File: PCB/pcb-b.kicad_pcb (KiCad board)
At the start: 2 copper layers, 117.6 x 58.2 mm, 81 parts, among them Q1 BC817, Q10 BC817, Q12 BC817, Q14 BC817, Q15 BC817, Q17 BC327, Q18 BC327, Q19 BC817, Q2 BC817, Q20 BC817, Q21 BC817, Q3 BC817, Q4 IRF4905, Q5 IRF4905, Q6 IRF4905, Q7 IRF4905, Q8 IRF4905, Q9 IRF4905, U1 L7805, U2 L7805, U3 L7805, U4 HK19F-DC12-SHG

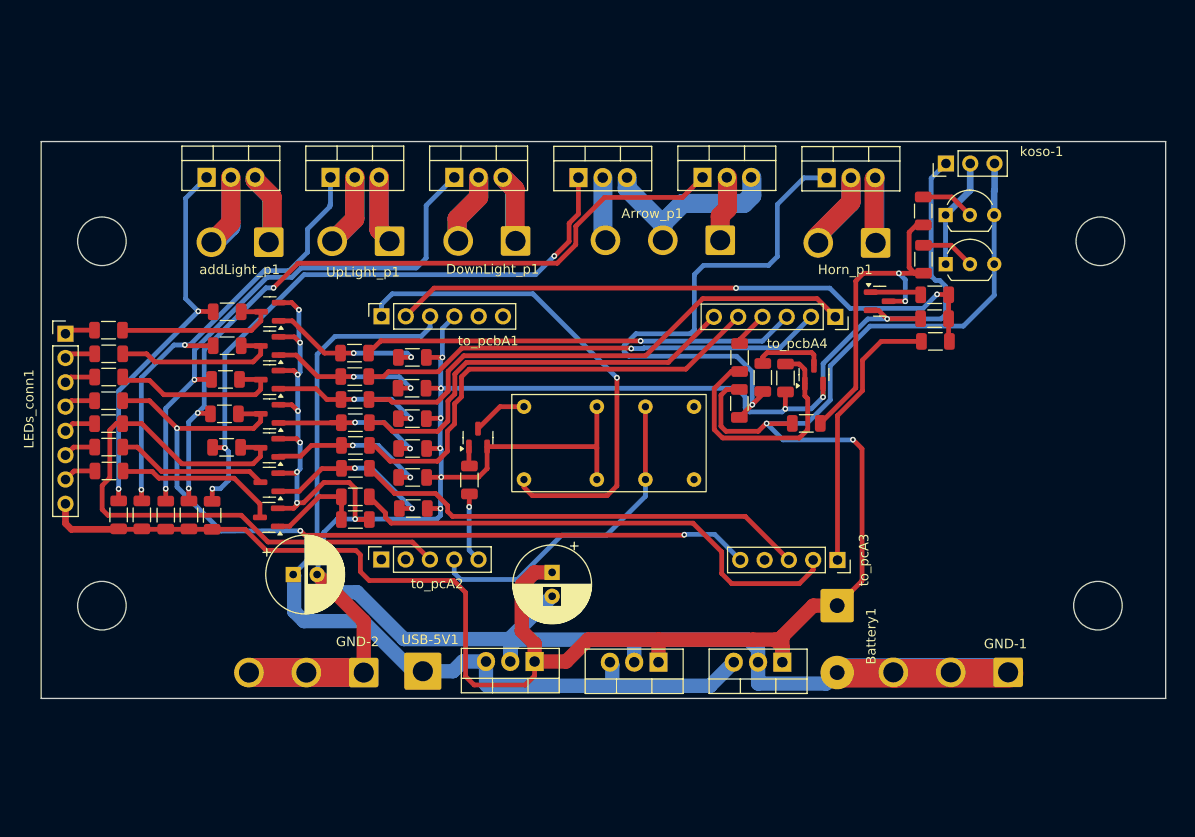
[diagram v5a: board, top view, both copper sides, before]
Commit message: SMD version using TPCA8120
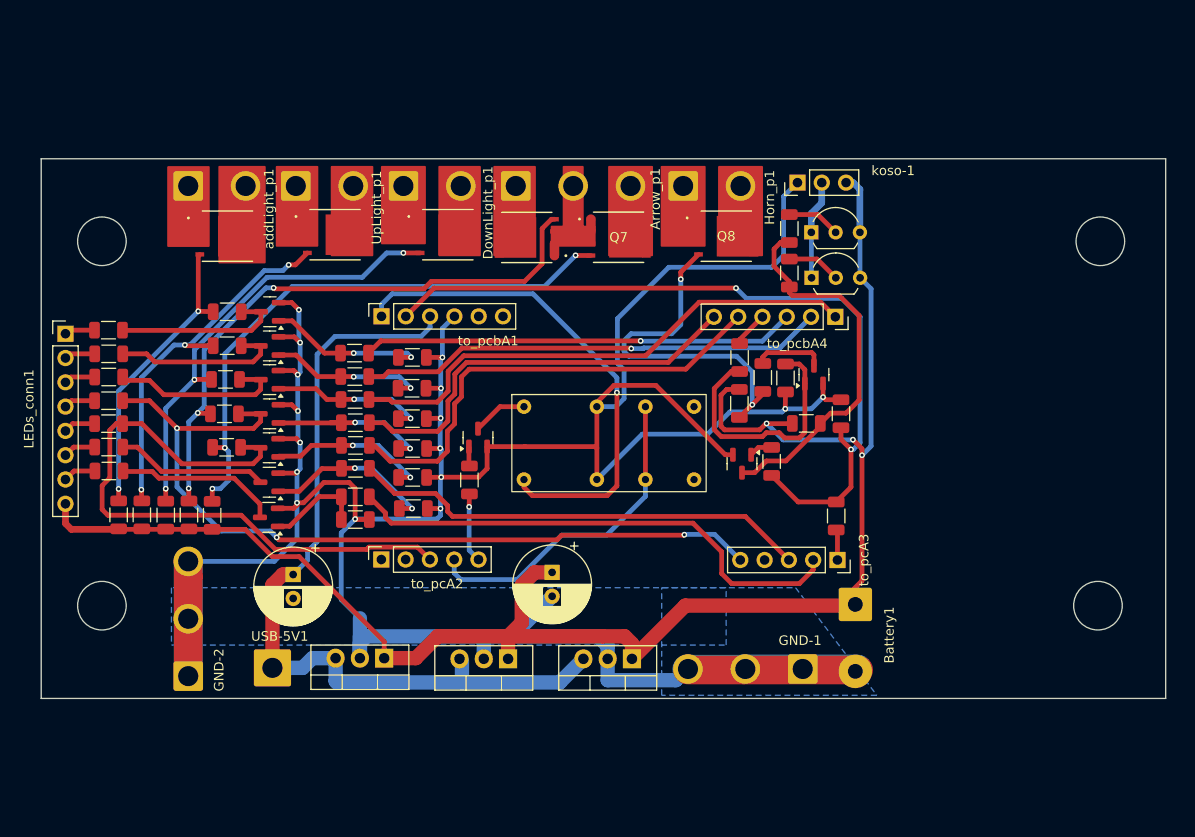
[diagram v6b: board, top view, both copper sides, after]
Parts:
- removed Q9: IRF4905, Package_TO_SOT_THT:TO-220-3_Vertical
- added Q11: TPCA8120,L1Q, TPCA8120:SOP Advance_TOS-L, F.Cu at (119.1, 78.3)
- Q4, Q5, Q6, Q7, Q8: value IRF4905 -> TPCA8120,L1Q; footprint Package_TO_SOT_THT:TO-220-3_Vertical -> TPCA8120:SOP Advance_TOS-L
- moved RA8 24.4 mm to (175.9, 101.9), turned to 90 degrees
- moved Q10 22.3 mm to (172.8, 102.1), turned to -90 degrees
- moved Arrow_p1 22.1 mm to (149.2, 73.1), turned to 0 degrees
- moved GND-1 21.5 mm to (179.2, 123.6)
- moved RA43 21.0 mm to (182.7, 107.6), turned to -90 degrees
- moved Horn_p1 21.0 mm to (166.7, 73.1), turned to 0 degrees
- moved GND-2 18.4 mm to (115.0, 124.3), turned to 90 degrees
- moved Q8 16.6 mm to (171.2, 78.3)
- moved U1 15.7 mm to (161.3, 122.5)
- moved U2 15.7 mm to (148.4, 122.5)
- moved U3 15.7 mm to (135.4, 122.5)
- moved USB-5V1 15.7 mm to (123.8, 123.5)
- moved koso-1 15.7 mm to (178.7, 72.8)
- moved Q4 14.7 mm to (130.3, 78.2)
- moved Q18 14.2 mm to (180.1, 78.0)
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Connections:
- Q4 pad 1: Net-(Q4-G) -> Net-(Q4-S_1)
- Q4 pad 2: Net-(Q4-D) -> Net-(Q4-S_1)
- Q4 pad 3: Net-(Q4-S) -> Net-(Q4-S_1)
- Q5 pad 1: Net-(Q5-G) -> Net-(DownLight_p1-Pin_1)
- Q5 pad 2: Net-(Q5-D) -> Net-(DownLight_p1-Pin_1)
- Q5 pad 3: Net-(Q5-S) -> Net-(DownLight_p1-Pin_1)
- Q6 pad 1: Net-(Q6-G) -> Net-(Arrow_p1-Pin_2)
- Q6 pad 2: Net-(DownLight_p1-Pin_2) -> Net-(Arrow_p1-Pin_2)
- Q6 pad 3: Net-(DownLight_p1-Pin_1) -> Net-(Arrow_p1-Pin_2)
- Q7 pad 1: Net-(Q7-G) -> Net-(Arrow_p1-Pin_2)
- Q7 pad 2: Net-(Arrow_p1-Pin_1) -> Net-(Arrow_p1-Pin_2)
- Q8 pad 1: Net-(Q8-G) -> Net-(Horn_p1-Pin_1)
- Q8 pad 2: Net-(Arrow_p1-Pin_3) -> Net-(Horn_p1-Pin_1)
- Q8 pad 3: Net-(Arrow_p1-Pin_2) -> Net-(Horn_p1-Pin_1)
- RA10 pad 2: Net-(Q4-G) -> Net-(Q11-G)
- RA11 pad 2: Net-(Q5-G) -> Net-(Q4-G)
- RA12 pad 2: Net-(Q6-G) -> Net-(Q5-G)
- RA13 pad 2: Net-(Q7-G) -> Net-(Q6-G)
- RA14 pad 2: Net-(Q8-G) -> Net-(Q7-G)
- RA15 pad 1: Net-(Q9-G) -> Net-(Q8-G)
- RA24 pad 2: Net-(Q4-G) -> Net-(Q11-G)
- RA25 pad 2: Net-(Q5-G) -> Net-(Q4-G)
- RA26 pad 2: Net-(Q6-G) -> Net-(Q5-G)
- RA27 pad 2: Net-(Q7-G) -> Net-(Q6-G)
- RA28 pad 2: Net-(Q8-G) -> Net-(Q7-G)
- RA42 pad 1: Net-(Q9-G) -> Net-(Q8-G)
- UpLight_p1 pad 1: Net-(Q5-S) -> Net-(Q4-S_1)
- UpLight_p1 pad 2: Net-(Q5-D) -> Net-(Q4-D_1)
- addLight_p1 pad 1: Net-(Q4-S) -> Net-(Q11-S_1)
- addLight_p1 pad 2: Net-(Q4-D) -> Net-(Q11-D_1)
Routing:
- net Net-(Q9-G): track 57.1 -> 0.00 mm, vias 1 -> 0
- net Net-(Q11-G): track 0.00 -> 31.0 mm, vias 0 -> 2
- net Net-(Q8-G): track 66.5 -> 37.3 mm, vias 3 -> 2
- net +12V: track 206.8 -> 179.3 mm, vias 2 -> 3
- net o_keepAlive: track 29.0 -> 3.20 mm
- net Net-(Arrow_p1-Pin_2): track 22.7 -> 2.54 mm
- net Net-(Q7-G): track 78.7 -> 60.7 mm
- net i_powerOFF: track 64.4 -> 81.1 mm
- net Net-(Q4-S): track 15.3 -> 0.00 mm
- net Net-(Q4-D): track 15.3 -> 0.00 mm
- net Net-(Q5-D): track 15.3 -> 0.00 mm
- net Net-(Q5-S): track 14.3 -> 0.00 mm
- net GND: track 360.4 -> 350.3 mm, vias 17 -> 16
- net Net-(Horn_p1-Pin_2): track 16.1 -> 7.73 mm
- net Net-(Q11-D_1): track 0.00 -> 7.98 mm
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- added copper zone on B.Cu, net GND
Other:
- board size 117.6 x 58.2 mm -> 117.6 x 56.4 mm

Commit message: Space optimization
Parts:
- moved Battery1 9.51 mm to (175.2, 116.3), turned to 0 degrees
- moved RA28 3.51 mm to (119.7, 104.8)
- moved RA27 3.43 mm to (117.2, 104.8)
- moved RA26 3.39 mm to (114.7, 104.8)
- moved RA25 3.37 mm to (112.2, 104.8)
- moved RA14 2.84 mm to (118.7, 97.6)
- moved C1 2.76 mm to (128.4, 112.6)
- moved GND-2 2.75 mm to (115.0, 121.6)
- moved RA24 2.35 mm to (106.7, 105.3), turned to 180 degrees
- moved RA13 2.33 mm to (118.7, 94.6)
- moved RA12 1.73 mm to (118.8, 91.6)
- moved C9 1.40 mm to (152.9, 112.1)
- moved RA11 1.20 mm to (119.0, 88.6)
- moved Arrow_p1 1.00 mm to (149.2, 74.1)
- moved DownLight_p1 1.00 mm to (137.4, 74.1)
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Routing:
- net Net-(Q5-G): track 47.0 -> 84.1 mm
- net c_rightArrow: track 66.4 -> 49.6 mm, vias 0 -> 2
- net tempPower: track 52.6 -> 36.8 mm
- net +12V: track 179.3 -> 193.1 mm, vias 3 -> 4
- net Net-(Q8-G): track 37.3 -> 27.1 mm
- net Net-(Q4-G): track 38.8 -> 34.0 mm
- net Net-(Q21-C): track 17.2 -> 20.8 mm
- net Net-(Q7-G): track 60.7 -> 57.4 mm
- net o_leftArrow: track 43.8 -> 46.4 mm
- net o_downLight: track 55.1 -> 57.4 mm
- net i_powerOFF: track 81.1 -> 83.3 mm
- net GND: track 350.3 -> 352.3 mm
- net +5V: track 91.0 -> 92.8 mm
- net o_rightArrow: track 48.6 -> 50.3 mm
- net Net-(Q20-C): track 15.9 -> 17.2 mm
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
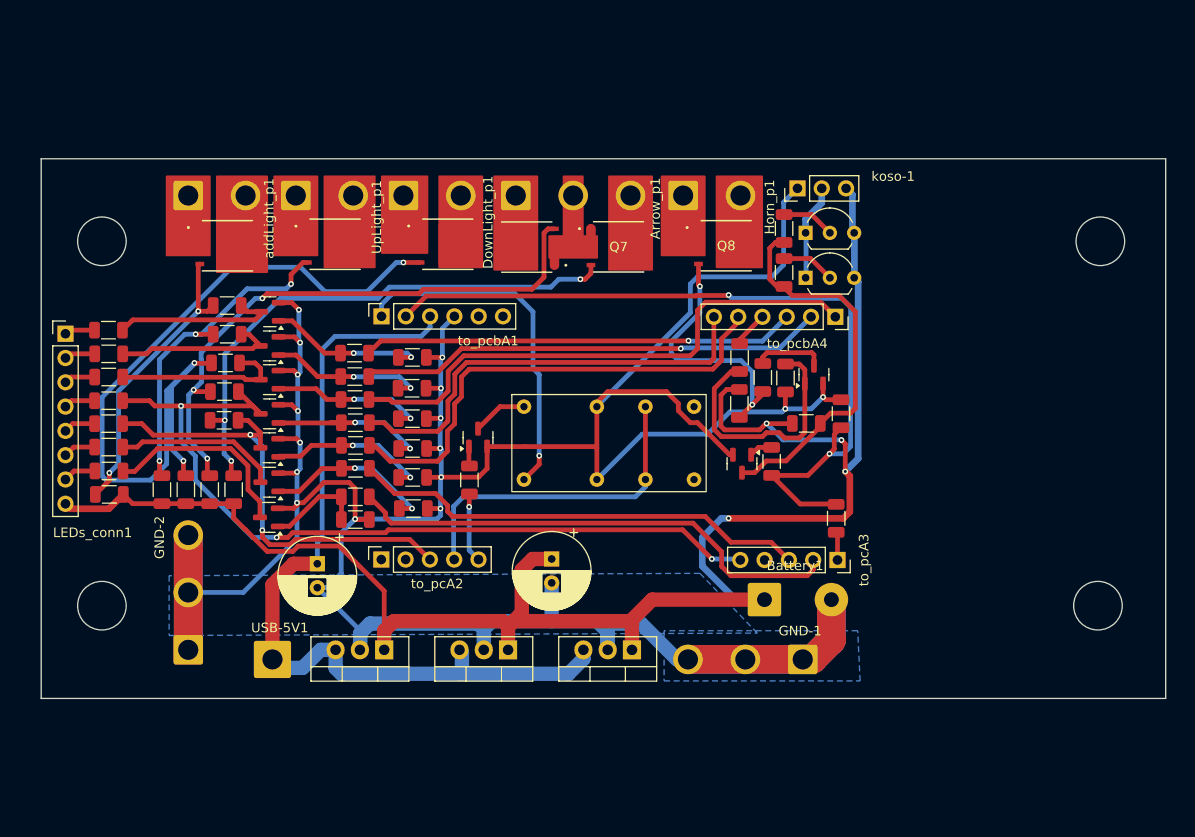
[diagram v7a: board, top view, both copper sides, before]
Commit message: Many changes
- The power drivers component has been implemented with TPCA8120 P-ch MOSfet
- The temp-power management has been moved from pcb-a to pcb-b
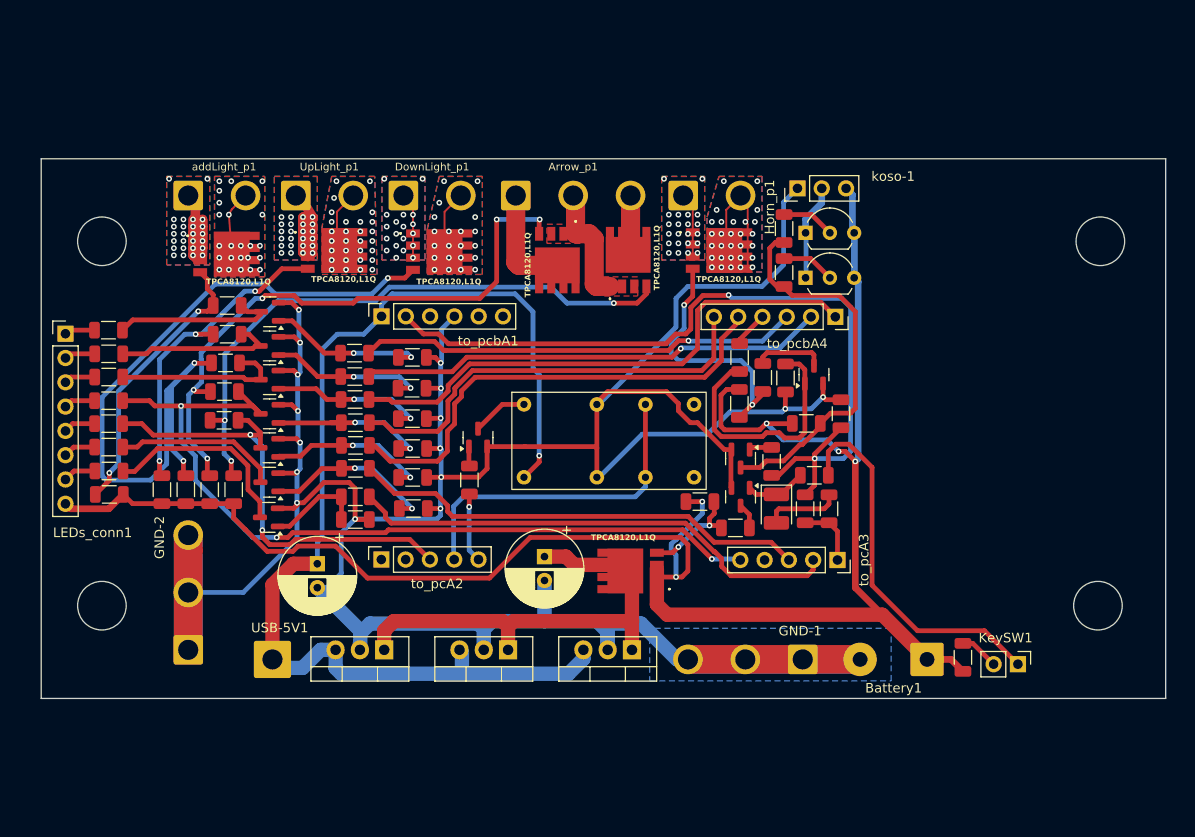
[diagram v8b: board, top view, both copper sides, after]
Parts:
- added D1: D_Small, Diode_SMD:D_1210_3225Metric_Pad1.42x2.65mm_HandSolder, F.Cu at (176.4, 106.8)
- added KeySW1: Conn_01x02, Connector_PinHeader_2.54mm:PinHeader_1x02_P2.54mm_Vertical, F.Cu at (201.7, 123.1)
- added Q13: TPCA8120,L1Q, TPCA8120:TPH4R003NLL1Q, F.Cu at (161.2, 113.3)
- added Q9: BC817, Package_TO_SOT_SMD:SOT-23, F.Cu at (172.7, 105.6)
- added R1: 5K, Resistor_SMD:R_1206_3216Metric, F.Cu at (195.9, 122.4)
- added R2: 10K, Resistor_SMD:R_1206_3216Metric, F.Cu at (168.4, 106.1)
- added R3: 33K, Resistor_SMD:R_1206_3216Metric, F.Cu at (172.2, 108.8)
- added R4: 5K, Resistor_SMD:R_1206_3216Metric, F.Cu at (180.4, 103.3)
- added R5: 5K, Resistor_SMD:R_1206_3216Metric, F.Cu at (181.9, 106.8)
- Q11, Q4, Q5, Q6, Q7, Q8: footprint TPCA8120:SOP Advance_TOS-L -> TPCA8120:TPH4R003NLL1Q
- RA10, RA11, RA12: value 240 -> 33K
- RA13, RA14: value 8K -> 33K
- RA15: value 8K -> 33k
- RA24, RA25, RA26, RA27, RA28: value 100K -> 10K
- RA42: value 8K -> 10k
- moved Battery1 18.1 mm to (192.2, 122.6), turned to 180 degrees
- moved Q6 3.48 mm to (153.5, 80.8)
- moved RA43 3.40 mm to (179.4, 106.8)
- moved Q7 1.71 mm to (160.9, 80.8)
- moved Q5 1.18 mm to (141.2, 80.0), turned to -90 degrees
- moved Q8 0.90 mm to (170.4, 79.8), turned to -90 degrees
- moved Q11 0.87 mm to (119.0, 80.2), turned to -90 degrees
- moved C9 0.79 mm to (152.2, 111.8)
- moved Q4 0.66 mm to (130.2, 79.8), turned to -90 degrees
- moved Q10 0.56 mm to (172.7, 101.6)
- moved U4 0.23 mm to (157.7, 106.1)
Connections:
- C1 pad 1: +5V -> tempPower
- C9 pad 1: +12V -> Net-(Q13-D_1)
- U1 pad 1: +12V -> Net-(Q13-D_1)
- U1 pad 3: +5V -> tempPower
- U2 pad 1: +12V -> Net-(Q13-D_1)
- U2 pad 3: +5V -> tempPower
- U3 pad 1: +12V -> Net-(Q13-D_1)
- U3 pad 3: +5V -> tempPower
- USB-5V1 pad 1: +5V -> tempPower
- to_pcbA1 pad 3: +5V -> unconnected-(to_pcbA1-Pin_3-Pad3)
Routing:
- net +5V: track 92.8 -> 0.00 mm
- net tempPower: track 36.8 -> 123.6 mm
- net Net-(Q13-D_1): track 0.00 -> 48.8 mm
- net Net-(KeySW1-Pin_1): track 0.00 -> 39.4 mm
- net +12V: track 193.1 -> 206.7 mm, vias 4 -> 5
- net Net-(Q4-S_1): track 6.23 -> 18.4 mm, vias 0 -> 24
- net Net-(Q11-S_1): track 6.39 -> 17.7 mm, vias 0 -> 26
- net Net-(Q13-G): track 0.00 -> 10.8 mm, vias 0 -> 2
- net Net-(Arrow_p1-Pin_2): track 2.54 -> 12.8 mm
- net Net-(D1-A): track 0.00 -> 8.00 mm
- net Net-(Horn_p1-Pin_2): track 7.73 -> 14.6 mm, vias 0 -> 29
- net Net-(D1-K): track 0.00 -> 6.41 mm
- net Net-(Q7-G): track 57.4 -> 63.6 mm
- net Net-(Arrow_p1-Pin_1): track 7.74 -> 12.7 mm
- net Net-(KeySW1-Pin_2): track 0.00 -> 4.11 mm
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- added copper zone on F.Cu, net Net-(Arrow_p1-Pin_2)
- added copper zone on B.Cu, net Net-(DownLight_p1-Pin_1)
- added copper zone on F.Cu, net Net-(DownLight_p1-Pin_1)
- added copper zone on B.Cu, net Net-(DownLight_p1-Pin_2)
- added copper zone on F.Cu, net Net-(DownLight_p1-Pin_2)
- added copper zone on B.Cu, net Net-(Horn_p1-Pin_1)
- added copper zone on F.Cu, net Net-(Horn_p1-Pin_1)
- added copper zone on B.Cu, net Net-(Horn_p1-Pin_2)
- added copper zone on F.Cu, net Net-(Horn_p1-Pin_2)
- added copper zone on B.Cu, net Net-(Q11-D_1)
- added copper zone on F.Cu, net Net-(Q11-D_1)
- added copper zone on B.Cu, net Net-(Q11-S_1)
- added copper zone on F.Cu, net Net-(Q11-S_1)
- added copper zone on B.Cu, net Net-(Q4-D_1)
- added copper zone on F.Cu, net Net-(Q4-D_1)
- added copper zone on B.Cu, net Net-(Q4-S_1)
- added copper zone on F.Cu, net Net-(Q4-S_1)
